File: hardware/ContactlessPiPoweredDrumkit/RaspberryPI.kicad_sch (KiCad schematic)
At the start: 6 parts, among them J1 Raspberry_Pi_1_2_3, U1 SN74LVC1T45DCK

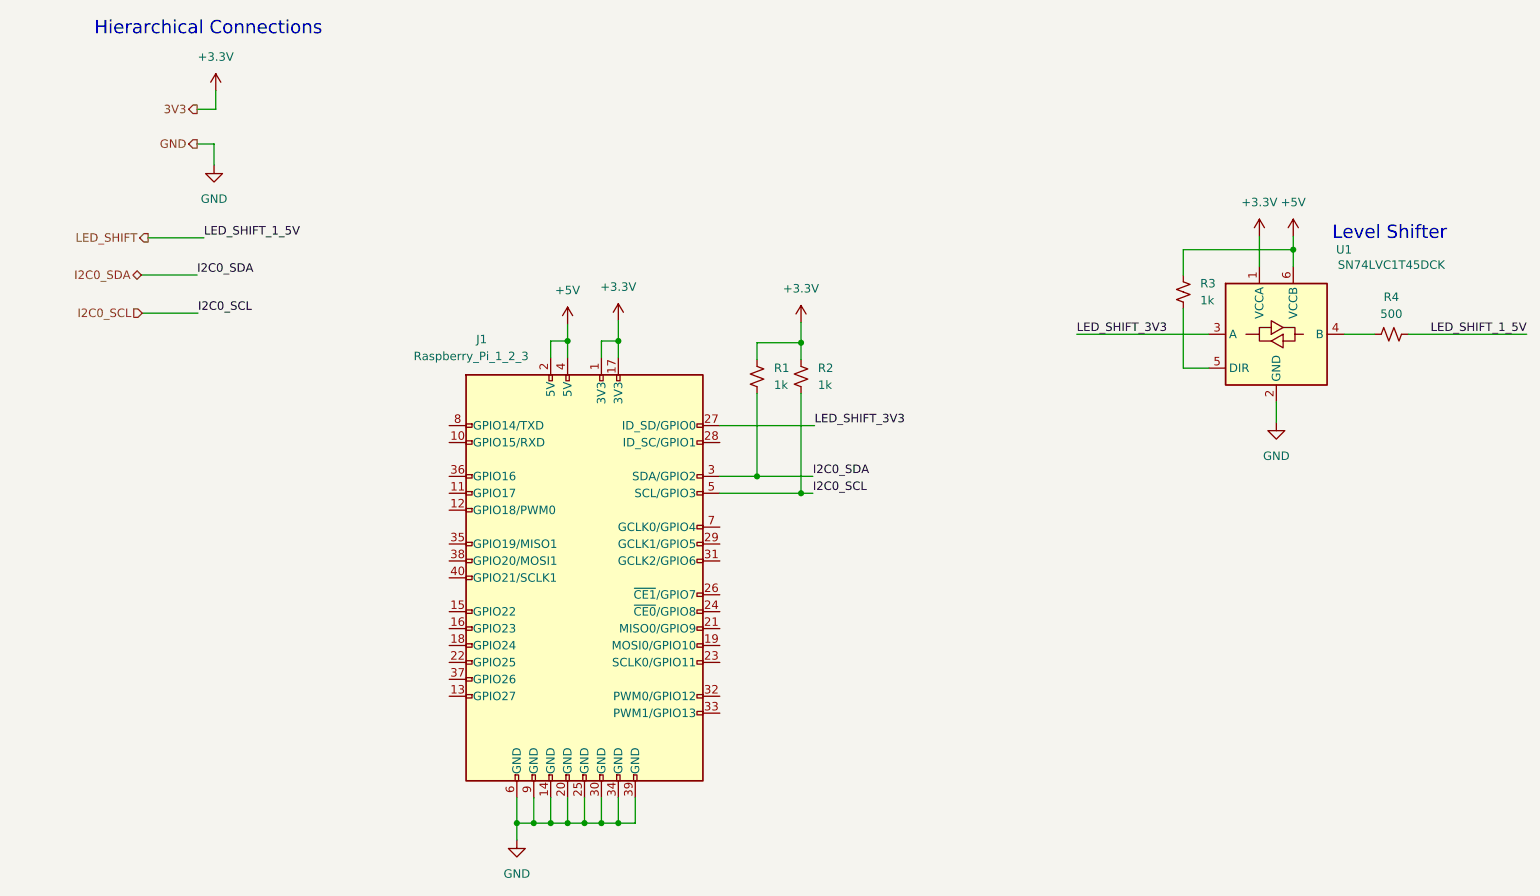
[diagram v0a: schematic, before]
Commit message: Complete PCB Layout
Completed PCB layout
Custom Artwork
Generate Gerbers
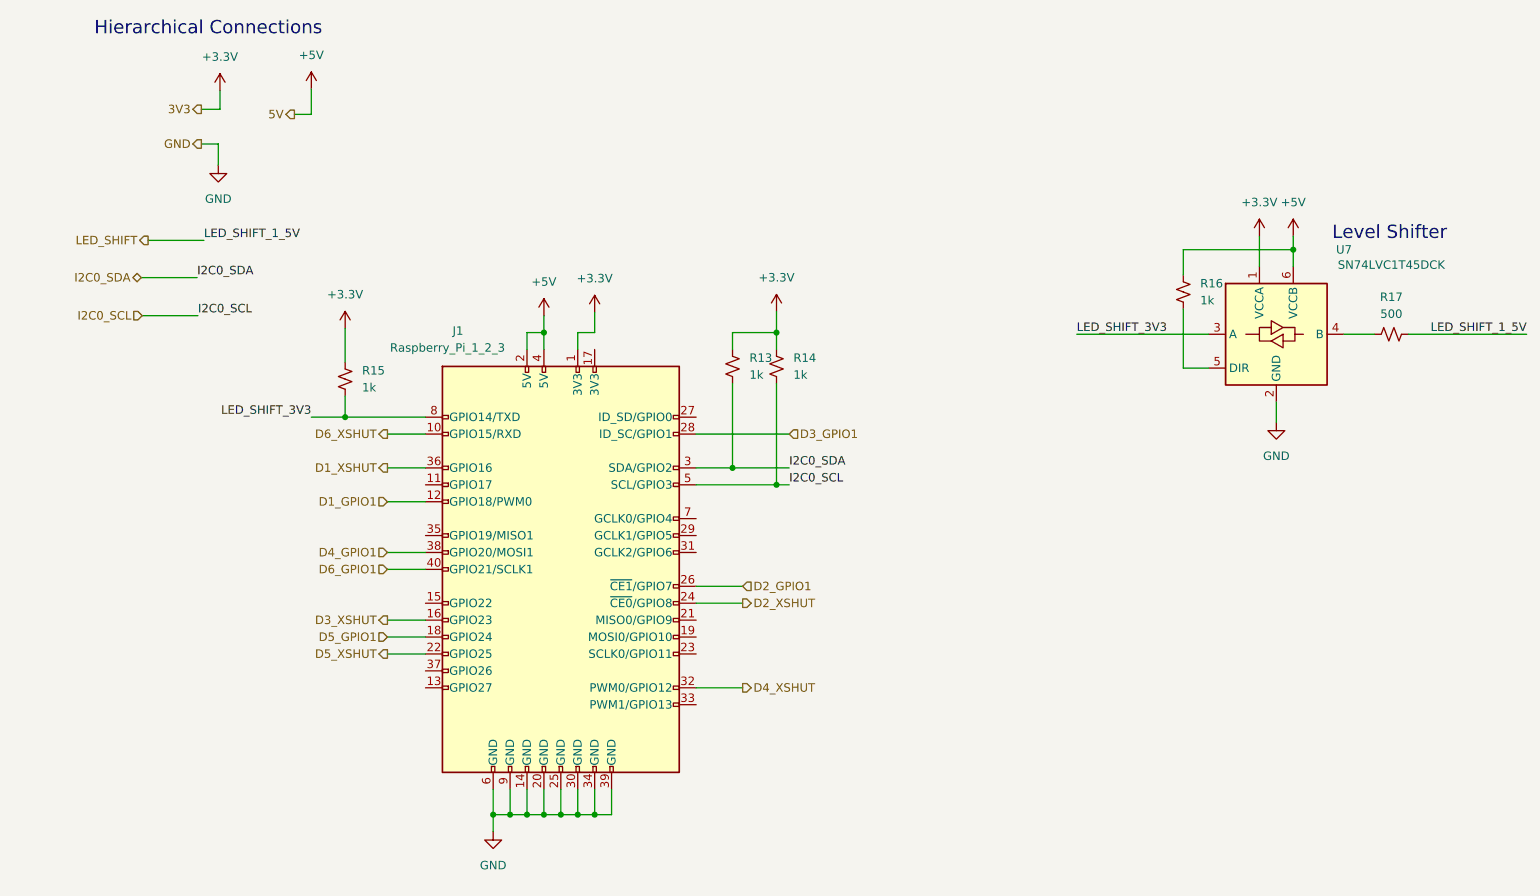
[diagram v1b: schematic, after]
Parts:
- added R15: 1k, Resistor_SMD:R_0603_1608Metric, symbol Device:R_Small_US
- R13: renamed from R1; footprint (none) -> Resistor_SMD:R_0603_1608Metric
- R14: renamed from R2; footprint (none) -> Resistor_SMD:R_0603_1608Metric
- R16: renamed from R3; footprint (none) -> Resistor_SMD:R_0603_1608Metric
- R17: renamed from R4; footprint (none) -> Resistor_SMD:R_0603_1608Metric
- renumbered U1 to U7
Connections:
- net +3.3V: now also R15.1; no longer J1.17 (3V3)
- net LED_SHIFT_3V3: now also J1.8 (GPIO14/TXD), R15.2; no longer J1.27 (ID_SD/GPIO0)
- net D6_XSHUT: now reaches J1.10 (GPIO15/RXD)
- net D1_GPIO1: now reaches J1.12 (GPIO18/PWM0)
- net D3_XSHUT: now reaches J1.16 (GPIO23)
- net D5_GPIO1: now reaches J1.18 (GPIO24)
- net D5_XSHUT: now reaches J1.22 (GPIO25)
- net D2_XSHUT: now reaches J1.24 (~{CE0}/GPIO8)
- net D2_GPIO1: now reaches J1.26 (~{CE1}/GPIO7)
- net D3_GPIO1: now reaches J1.28 (ID_SC/GPIO1)
- net D4_XSHUT: now reaches J1.32 (PWM0/GPIO12)
- net D1_XSHUT: now reaches J1.36 (GPIO16)
- net D4_GPIO1: now reaches J1.38 (GPIO20/MOSI1)
- net D6_GPIO1: now reaches J1.40 (GPIO21/SCLK1)
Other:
- moved on the sheet: J1, R13, R14

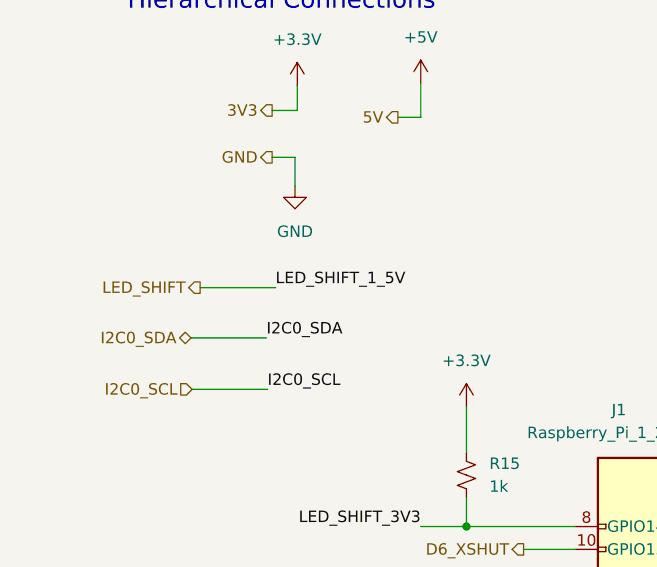
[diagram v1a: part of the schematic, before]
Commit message: Reviewed PCB DRC
Reduced constraint size from .3mm to .25mm
Move pullup resistors slightly
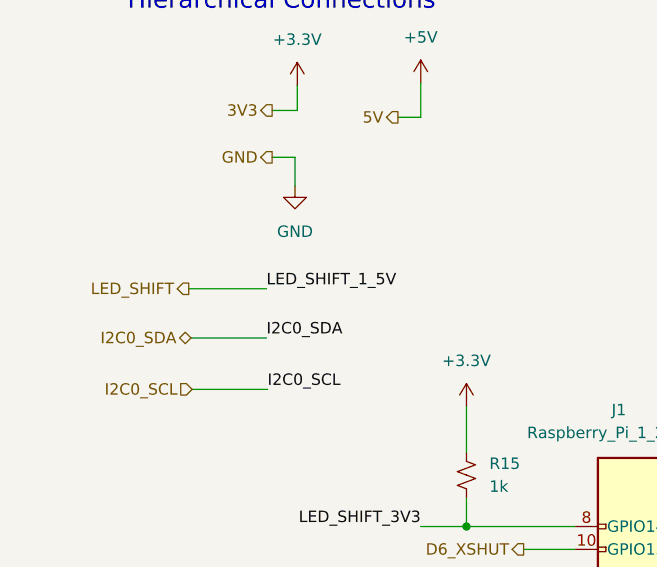
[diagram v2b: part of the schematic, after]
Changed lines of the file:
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@@
     (stroke (width 0) (type default))
   )
-  (wire (pts (xy 33.274 51.943) (xy 41.656 51.943))
+  (wire (pts (xy 32.004 52.07) (xy 40.64 52.07))
     (stroke (width 0) (type default))
   )
@@
     (effects (font (size 1.27 1.27)) (justify left bottom))
   )
-  (label "LED_SHIFT_1_5V" (at 41.656 51.943 0) (fields_autoplaced)
+  (label "LED_SHIFT_1_5V" (at 40.64 52.07 0) (fields_autoplaced)
     (effects (font (size 1.27 1.27)) (justify left bottom))
   )
@@
     (effects (font (size 1.27 1.27)) (justify right))
   )
-  (hierarchical_label "LED_SHIFT" (shape output) (at 33.274 51.943 180) (fields_autoplaced)
+  (hierarchical_label "LED_SHIFT" (shape output) (at 32.004 52.07 180) (fields_autoplaced)
     (effects (font (size 1.27 1.27)) (justify right))
   )
